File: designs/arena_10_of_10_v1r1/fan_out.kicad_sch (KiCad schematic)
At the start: 0 parts

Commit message: Fixed some issues with analog subsystem and added ethernet connection.
Added +/-15V power rails for bipolar analog inputs. Added 10V reference
voltage. Fixed connections for ethernet connection to teensy.
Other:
- note added: "Post-Fanout Signals"
- note added: "Pre-fanout signals"
- note added: "Singals to/from Teensy"
- note removed: "Singals from/to Teensy"
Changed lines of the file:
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@@
+		)
+	)
+	(text "Pre-fanout signals"
+		(exclude_from_sim no)
+		(at 40.386 120.396 0)
+		(effects
+			(font
+				(size 1.905 1.905)
+				(thickness 0.508)
+				(bold yes)
+			)
 		)
 	)
@@
 		)
 	)
-	(text "Singals from/to Teensy"
-		(exclude_from_sim no)
-		(at 40.894 19.304 0)
+	(text "SPI Bus B1 MOSI\nfor columns P6-P10"
+		(exclude_from_sim no)
+		(at 426.466 97.028 0)
+		(effects
+			(font
+				(size 1.27 1.27)
+			)
+			(justify left)
+		)
+	)
+	(text "SPI Bus B0 SCK\nfor columns P1-P5"
+		(exclude_from_sim no)
+		(at 426.466 36.068 0)
+		(effects
+			(font
+				(size 1.27 1.27)
+			)
+			(justify left)
+		)
+	)
+	(text "SPI Bus B0 MOSI\nfor columns P1-P5"
+		(exclude_from_sim no)
+		(at 426.466 51.308 0)
+		(effects
+			(font
+				(size 1.27 1.27)
+			)
+			(justify left)
+		)
+	)
+	(text "CS for column P1"
+		(exclude_from_sim no)
+		(at 434.848 126.492 0)
+		(effects
+			(font
+				(size 1.27 1.27)
+			)
+		)
+	)
+	(text "CS for column P5"
+		(exclude_from_sim no)
+		(at 434.848 176.784 0)
+		(effects
+			(font
+				(size 1.27 1.27)
+			)
+		)
+	)
+	(text "CS for column P8"
+		(exclude_from_sim no)
+		(at 435.102 216.408 0)
+		(effects
+			(font
+				(size 1.27 1.27)
+			)
+		)
+	)
+	(text "CS for column P3"
+		(exclude_from_sim no)
+		(at 435.102 151.384 0)
+		(effects
+			(font
+				(size 1.27 1.27)
+			)
+		)
+	)
+	(text "SPI Bus B1 SCK\nfor columns P6-P10"
+		(exclude_from_sim no)
+		(at 426.466 81.788 0)
+		(effects
+			(font
+				(size 1.27 1.27)
+			)
+			(justify left)
+		)
+	)
+	(text "External Interrupt"
+		(exclude_from_sim no)
+		(at 32.766 104.14 0)
+		(effects
+			(font
+				(size 1.27 1.27)
+			)
+			(justify right)
+		)
+	)
+	(text "External Interrupts\nfor columns P1-P10"
+		(exclude_from_sim no)
+		(at 426.974 260.604 0)
+		(effects
+			(font
+				(size 1.27 1.27)
+			)
+			(justify left)
+		)
+	)
+	(text "CS for column P7"
+		(exclude_from_sim no)
+		(at 435.102 203.454 0)
+		(effects
+			(font
+				(size 1.27 1.27)
+			)
+		)
+	)
+	(text "Post-Fanout Signals"
+		(exclude_from_sim no)
+		(at 420.37 286.004 0)
+		(effects
+			(font
+				(size 1.905 1.905)
+				(thickness 0.508)
+				(bold yes)
+			)
+		)
+	)
+	(text "CS for column P4"
+		(exclude_from_sim no)
+		(at 435.102 164.592 0)
+		(effects
+			(font
+				(size 1.27 1.27)
+			)
+		)
+	)
+	(text "CS for column P10"
+		(exclude_from_sim no)
+		(at 435.102 241.554 0)
+		(effects
+			(font
+				(size 1.27 1.27)
+			)
+		)
+	)
+	(text "SPI Bus B0 MISO\nfor columns P1-P5"
+		(exclude_from_sim no)
+		(at 426.466 65.786 0)
+		(effects
+			(font
+				(size 1.27 1.27)
+			)
+			(justify left)
+		)
+	)
+	(text "CS for column P9"
+		(exclude_from_sim no)
+		(at 434.848 228.854 0)
+		(effects
+			(font
+				(size 1.27 1.27)
+			)
+		)
+	)
+	(text "CS for column P2"
+		(exclude_from_sim no)
+		(at 434.848 138.684 0)
+		(effects
+			(font
+				(size 1.27 1.27)
+			)
+		)
+	)
+	(text "Singals to/from Teensy"
+		(exclude_from_sim no)
+		(at 42.418 21.082 0)
 		(effects
 			(font
@@
 			)
 		)
-	)
-	(text "SPI Bus B1 MOSI\nfor columns P6-P10"
-		(exclude_from_sim no)
-		(at 426.466 97.028 0)
-		(effects
-			(font
-				(size 1.27 1.27)
-			)
-			(justify left)
-		)
-	)
-	(text "SPI Bus B0 SCK\nfor columns P1-P5"
-		(exclude_from_sim no)
-		(at 426.466 36.068 0)
-		(effects
-			(font
-				(size 1.27 1.27)
-			)
-			(justify left)
-		)
-	)
-	(text "SPI Bus B0 MOSI\nfor columns P1-P5"
-		(exclude_from_sim no)
-		(at 426.466 51.308 0)
-		(effects
-			(font
-				(size 1.27 1.27)
-			)
-			(justify left)
-		)
-	)
-	(text "CS for column P1"
-		(exclude_from_sim no)
-		(at 434.848 126.492 0)
-		(effects
-			(font
-				(size 1.27 1.27)
-			)
-		)
-	)
-	(text "CS for column P5"
-		(exclude_from_sim no)
-		(at 434.848 176.784 0)
-		(effects
-			(font
-				(size 1.27 1.27)
-			)
-		)
-	)
-	(text "CS for column P8"
-		(exclude_from_sim no)
-		(at 435.102 216.408 0)
-		(effects
-			(font
-				(size 1.27 1.27)
-			)
-		)
-	)
-	(text "CS for column P3"
-		(exclude_from_sim no)
-		(at 435.102 151.384 0)
-		(effects
-			(font
-				(size 1.27 1.27)
-			)
-		)
-	)
-	(text "SPI Bus B1 SCK\nfor columns P6-P10"
-		(exclude_from_sim no)
-		(at 426.466 81.788 0)
-		(effects
-			(font
-				(size 1.27 1.27)
-			)
-			(justify left)
-		)
-	)
-	(text "External Interrupt"
-		(exclude_from_sim no)
-		(at 32.766 104.14 0)
-		(effects
-			(font
-				(size 1.27 1.27)
-			)
-			(justify right)
-		)
-	)
-	(text "External Interrupts\nfor columns P1-P10"
-		(exclude_from_sim no)
-		(at 426.974 260.604 0)
-		(effects
-			(font
-				(size 1.27 1.27)
-			)
-			(justify left)
-		)
-	)
-	(text "CS for column P7"
-		(exclude_from_sim no)
-		(at 435.102 203.454 0)
-		(effects
-			(font
-				(size 1.27 1.27)
-			)
-		)
-	)
-	(text "CS for column P4"
-		(exclude_from_sim no)
-		(at 435.102 164.592 0)
-		(effects
-			(font
-				(size 1.27 1.27)
-			)
-		)
-	)
-	(text "CS for column P10"
-		(exclude_from_sim no)
-		(at 435.102 241.554 0)
-		(effects
-			(font
-				(size 1.27 1.27)
-			)
-		)
-	)
-	(text "SPI Bus B0 MISO\nfor columns P1-P5"
-		(exclude_from_sim no)
-		(at 426.466 65.786 0)
-		(effects
-			(font
-				(size 1.27 1.27)
-			)
-			(justify left)
-		)
-	)
-	(text "CS for column P9"
-		(exclude_from_sim no)
-		(at 434.848 228.854 0)
-		(effects
-			(font
-				(size 1.27 1.27)
-			)
-		)
-	)
-	(text "CS for column P2"
-		(exclude_from_sim no)
-		(at 434.848 138.684 0)
-		(effects
-			(font
-				(size 1.27 1.27)
-			)
-		)

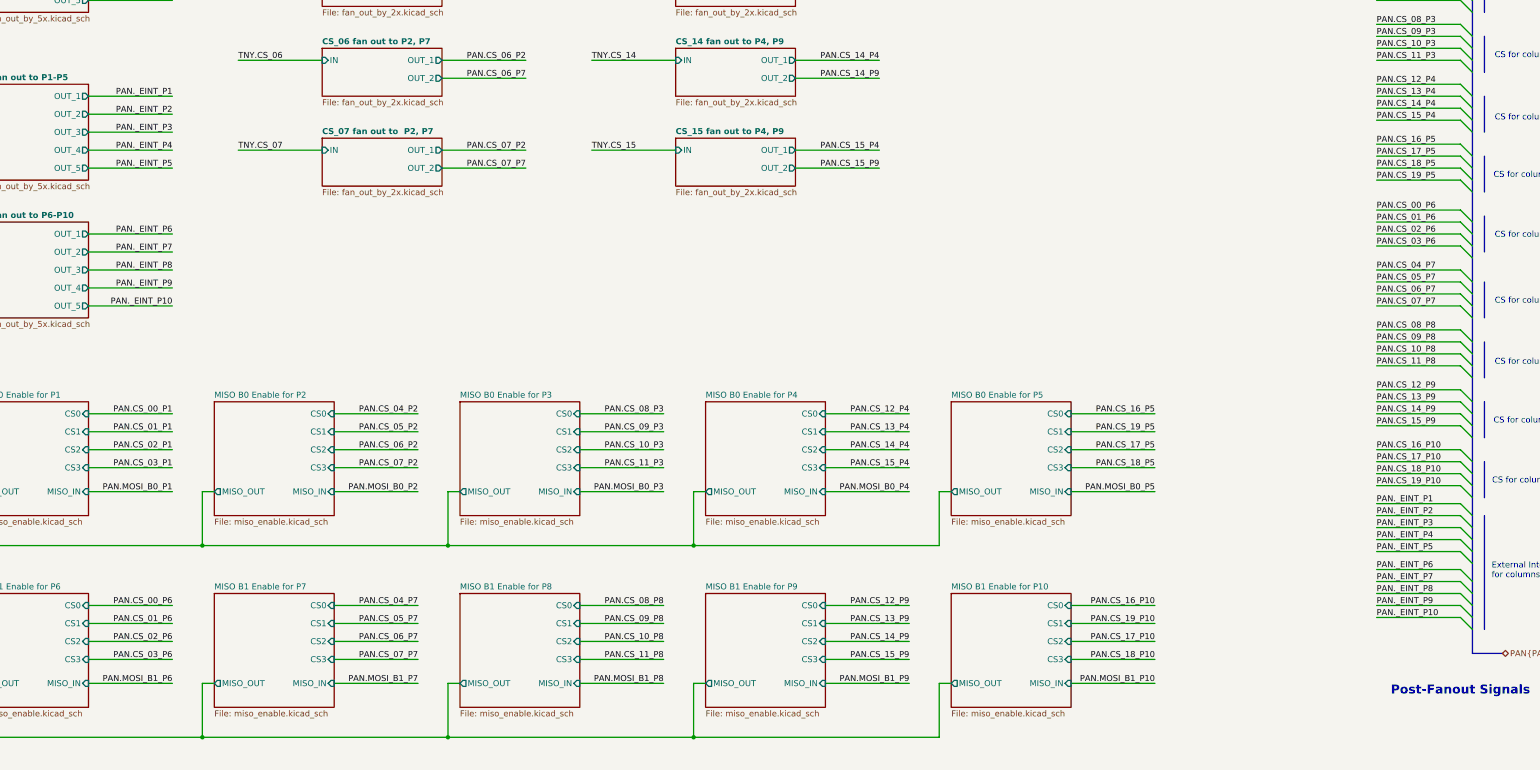
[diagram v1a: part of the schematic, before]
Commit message: Working through schematic design rule check.
Just some power issues remaing.
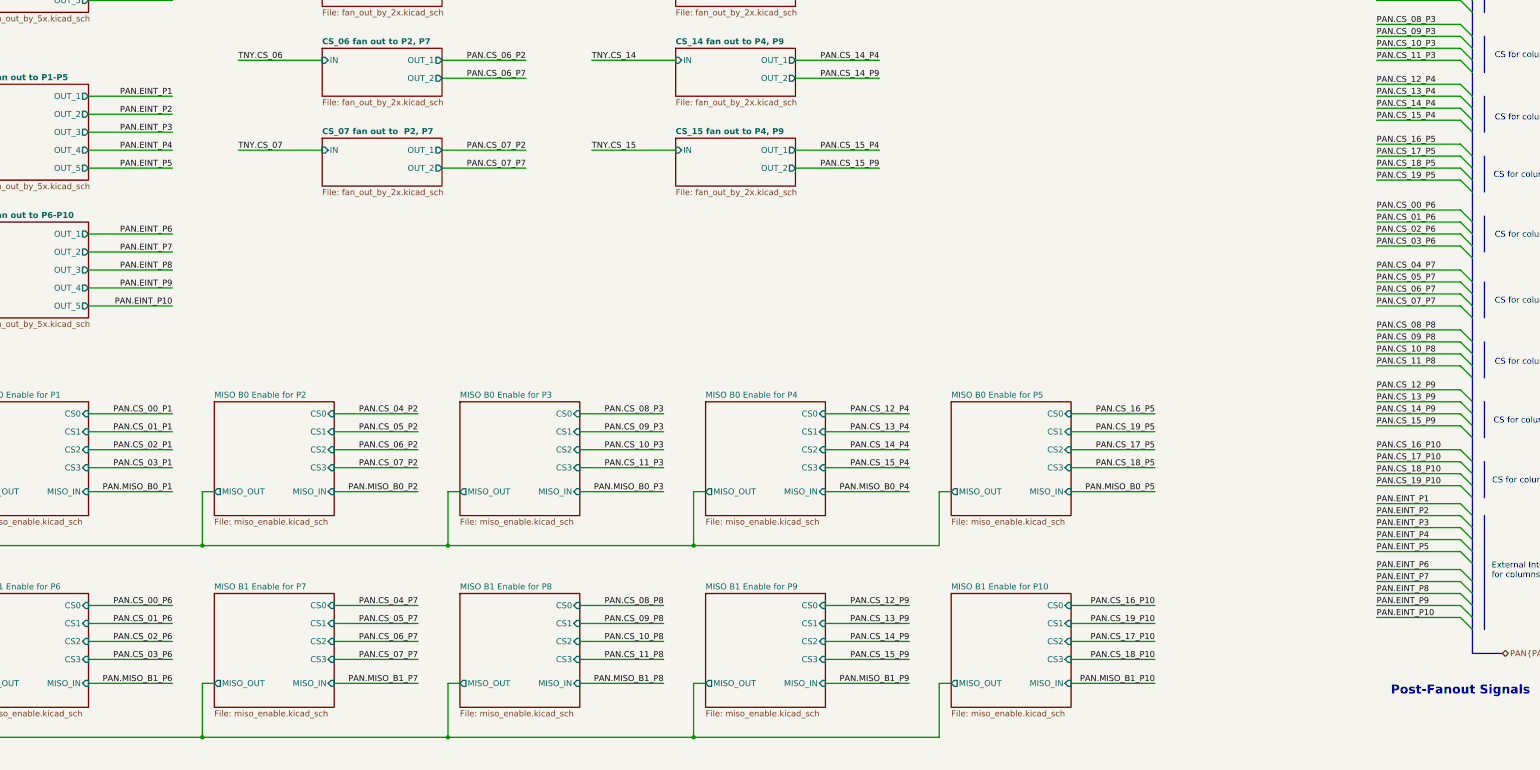
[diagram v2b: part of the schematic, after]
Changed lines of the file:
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@@
 			"EINT_P8" "EINT_P9" "EINT_P10" "MISO_B0_P1" "MISO_B0_P2" "MISO_B0_P3"
 			"MISO_B0_P4" "MISO_B0_P5" "MISO_B1_P6" "MISO_B1_P7" "MISO_B1_P8" "MISO_B1_P9"
-			"MISO_B1_P10"
+			"MISO_B1_P10" "CS_18_P10"
 		)
 	)
@@
 		)
 	)
+	(label "PAN.EINT_P4"
+		(at 147.32 171.45 180)
+		(effects
+			(font
+				(size 1.27 1.27)
+			)
+			(justify right bottom)
+		)
+	)
 	(label "PAN.CS_09_P8"
 		(at 297.18 50.8 180)
@@
 		)
 	)
+	(label "PAN.EINT_P7"
+		(at 147.32 193.04 180)
+		(effects
+			(font
+				(size 1.27 1.27)
+			)
+			(justify right bottom)
+		)
+	)
 	(label "PAN.CS_19_P10"
 		(at 372.11 88.9 180)
@@
 		)
 	)
+	(label "PAN.EINT_P1"
+		(at 147.32 160.02 180)
+		(effects
+			(font
+				(size 1.27 1.27)
+			)
+			(justify right bottom)
+		)
+	)
 	(label "PAN.CS_18_P5"
 		(at 402.59 175.26 0)
@@
 		)
 	)
+	(label "PAN.EINT_P2"
+		(at 147.32 163.83 180)
+		(effects
+			(font
+				(size 1.27 1.27)
+			)
+			(justify right bottom)
+		)
+	)
 	(label "PAN.MISO_B0_P1"
 		(at 402.59 58.42 0)
@@
 		)
 	)
-	(label "PAN._EINT_P2"
-		(at 147.32 163.83 180)
+	(label "PAN.EINT_P5"
+		(at 147.32 175.26 180)
 		(effects
 			(font
@@
 		)
 	)
-	(label "PAN._EINT_P6"
-		(at 147.32 189.23 180)
-		(effects
-			(font
-				(size 1.27 1.27)
-			)
-			(justify right bottom)
-		)
-	)
 	(label "PAN.MOSI_B1_P10"
 		(at 147.32 139.7 180)
@@
 		)
 	)
-	(label "PAN._EINT_P8"
+	(label "PAN.EINT_P8"
 		(at 402.59 265.43 0)
 		(effects
@@
 		)
 	)
+	(label "PAN.EINT_P3"
+		(at 147.32 167.64 180)
+		(effects
+			(font
+				(size 1.27 1.27)
+			)
+			(justify right bottom)
+		)
+	)
 	(label "TNY.CS_11"
 		(at 58.42 76.2 180)
@@
 		)
 	)
+	(label "PAN.EINT_P8"
+		(at 147.32 196.85 180)
+		(effects
+			(font
+				(size 1.27 1.27)
+			)
+			(justify right bottom)
+		)
+	)
 	(label "PAN.CS_07_P7"
 		(at 199.39 279.4 180)
@@
 		)
 	)
-	(label "PAN._EINT_P10"
+	(label "PAN.EINT_P10"
 		(at 402.59 270.51 0)
 		(effects
@@
 		)
 	)
-	(label "PAN.MOSI_B1_P6"
+	(label "PAN.MISO_B1_P6"
 		(at 147.32 284.48 180)
 		(effects
@@
 		)
 	)
-	(label "PAN.MOSI_B0_P3"
+	(label "PAN.MISO_B0_P3"
 		(at 251.46 243.84 180)
 		(effects
@@
 		)
 	)
-	(label "PAN._EINT_P5"
-		(at 147.32 175.26 180)
-		(effects
-			(font
-				(size 1.27 1.27)
-			)
-			(justify right bottom)
-		)
-	)
 	(label "PAN.MOSI_B0_P2"
 		(at 402.59 45.72 0)
@@
 		)
 	)
-	(label "PAN._EINT_P4"
-		(at 147.32 171.45 180)
+	(label "PAN.CS_01_P1"
+		(at 222.25 46.99 180)
 		(effects
 			(font
@@
 		)
 	)
-	(label "PAN.CS_01_P1"
-		(at 222.25 46.99 180)
+	(label "PAN.CS_18_P10"
+		(at 402.59 240.03 0)
 		(effects
 			(font
 				(size 1.27 1.27)
 			)
-			(justify right bottom)
+			(justify left bottom)
 		)
 	)
@@
 		)
 	)
-	(label "PAN._EINT_P2"
+	(label "PAN.EINT_P2"
 		(at 402.59 248.92 0)
 		(effects
@@
 		)
 	)
-	(label "PAN.CS_18_P10"
-		(at 402.59 240.03 0)
-		(effects
-			(font
-				(size 1.27 1.27)
-			)
-			(justify left bottom)
-		)
-	)
 	(label "TNY.CS_18"
 		(at 311.15 66.04 0)
@@
 		)
 	)
-	(label "PAN._EINT_P5"
+	(label "PAN.EINT_P5"
 		(at 402.59 256.54 0)
 		(effects
@@
 		)
 	)
-	(label "PAN._EINT_P4"
+	(label "PAN.EINT_P4"
 		(at 402.59 254 0)
 		(effects
@@
 		)
 	)
-	(label "PAN.MOSI_B1_P8"
+	(label "PAN.MISO_B1_P8"
 		(at 251.46 284.48 180)
 		(effects
@@
 		)
 	)
-	(label "PAN.MOSI_B1_P7"
+	(label "PAN.MISO_B1_P7"
 		(at 199.39 284.48 180)
 		(effects
@@
 		)
 	)
-	(label "PAN._EINT_P9"
-		(at 147.32 200.66 180)
-		(effects
-			(font
-				(size 1.27 1.27)
-			)
-			(justify right bottom)
-		)
-	)
 	(label "TNY.CS_07"
 		(at 58.42 66.04 180)
@@
 		)
 	)
-	(label "PAN._EINT_P9"
+	(label "PAN.EINT_P9"
 		(at 402.59 267.97 0)
 		(effects
@@
 		)
 	)
-	(label "PAN._EINT_P1"
-		(at 147.32 160.02 180)
-		(effects
-			(font
-				(size 1.27 1.27)
-			)
-			(justify right bottom)
-		)
-	)
 	(label "TNY.CS_17"
 		(at 58.42 91.44 180)
@@
 		)
 	)
-	(label "PAN._EINT_P1"
+	(label "PAN.EINT_P1"
 		(at 402.59 246.38 0)
 		(effects
@@
 		)
 	)
-	(label "PAN._EINT_P7"
+	(label "PAN.EINT_P7"
 		(at 402.59 262.89 0)
 		(effects
@@
 		)
 	)
-	(label "PAN.MOSI_B0_P4"
+	(label "PAN.MISO_B0_P4"
 		(at 303.53 243.84 180)
 		(effects
@@
 		)
 	)
-	(label "PAN.MOSI_B0_P1"
+	(label "PAN.MISO_B0_P1"
 		(at 147.32 243.84 180)
 		(effects
@@
 		)
 	)
-	(label "PAN._EINT_P10"
-		(at 147.32 204.47 180)
-		(effects
-			(font
-				(size 1.27 1.27)
-			)
-			(justify right bottom)
-		)
-	)
 	(label "PAN.MISO_B1_P6"
 		(at 402.59 104.14 0)
@@
 		)
 	)
-	(label "PAN.MOSI_B0_P5"
+	(label "PAN.MISO_B0_P5"
 		(at 355.6 243.84 180)
 		(effects
@@
 		)
 	)
+	(label "PAN.EINT_P10"
+		(at 147.32 204.47 180)
+		(effects
+			(font
+				(size 1.27 1.27)
+			)
+			(justify right bottom)
+		)
+	)
 	(label "PAN.SCK_B0_P4"
 		(at 147.32 39.37 180)
@@
 		)
 	)
-	(label "PAN.MOSI_B0_P2"
+	(label "PAN.MISO_B0_P2"
 		(at 199.39 243.84 180)
 		(effects
@@
 		)
 	)
-	(label "PAN._EINT_P6"
+	(label "PAN.EINT_P6"
 		(at 402.59 260.35 0)
 		(effects
@@
 		)
 	)
-	(label "PAN.MOSI_B1_P10"
+	(label "PAN.MISO_B1_P10"
 		(at 355.6 284.48 180)
 		(effects
@@
 		)
 	)
-	(label "PAN._EINT_P3"
+	(label "PAN.EINT_P3"
 		(at 402.59 251.46 0)
 		(effects
@@
 		)
 	)
-	(label "PAN._EINT_P3"
-		(at 147.32 167.64 180)
+	(label "PAN.EINT_P6"
+		(at 147.32 189.23 180)
 		(effects
 			(font
@@
 		)
 	)
-	(label "PAN._EINT_P7"
-		(at 147.32 193.04 180)
-		(effects
-			(font
-				(size 1.27 1.27)
-			)
-			(justify right bottom)
-		)
-	)
 	(label "PAN.CS_02_P6"
 		(at 147.32 275.59 180)
@@
 		)
 	)
-	(label "PAN._EINT_P8"
-		(at 147.32 196.85 180)
-		(effects
-			(font
-				(size 1.27 1.27)
-			)
-			(justify right bottom)
-		)
-	)
 	(label "TNY.CS_05"
 		(at 161.29 133.35 0)
@@
 		)
 	)
-	(label "PAN.MOSI_B1_P9"
+	(label "PAN.MISO_B1_P9"
 		(at 303.53 284.48 180)
 		(effects
@@
 		)
 	)
+	(label "PAN.EINT_P9"
+		(at 147.32 200.66 180)
+		(effects
+			(font
+				(size 1.27 1.27)
+			)
+			(justify right bottom)
+		)
+	)
